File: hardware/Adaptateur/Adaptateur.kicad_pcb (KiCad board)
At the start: 2 copper layers, 74 x 42 mm, 16 parts, among them J1 USB_B, U1 FT232RL, U2 XBee, U3 IFX27001TFV33

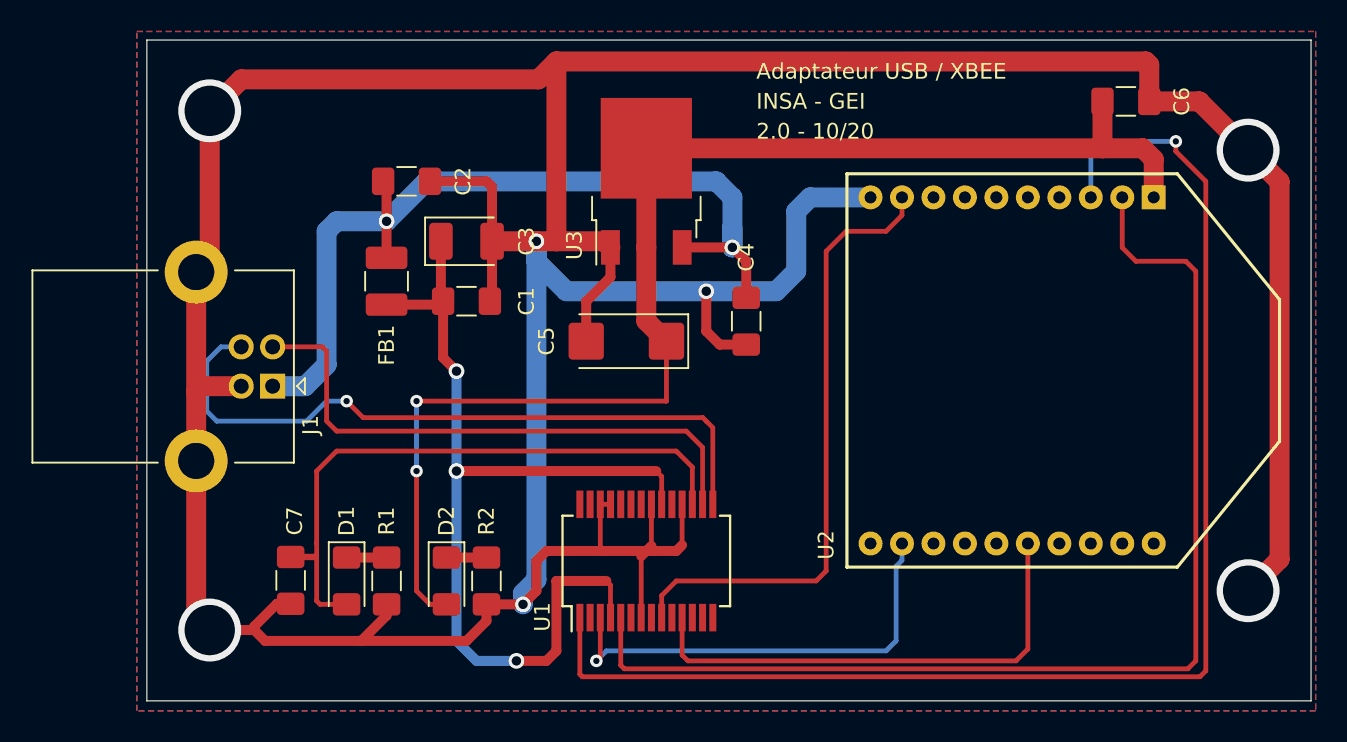
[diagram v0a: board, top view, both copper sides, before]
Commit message: correction et mise à jour adaptateur USB XBEE premiere version (boitier gris)
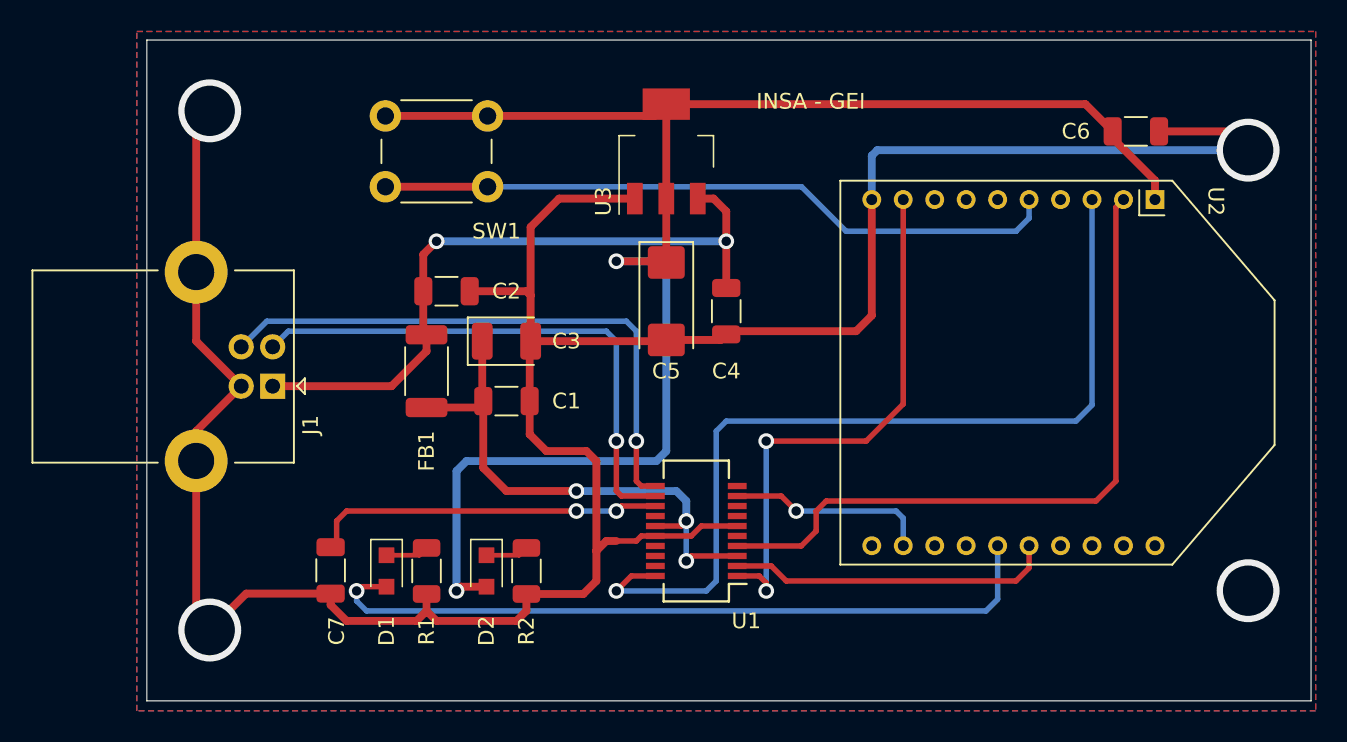
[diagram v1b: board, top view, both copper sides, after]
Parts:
- added SW1: SW_Push_SPDT, Button_Switch_THT:SW_PUSH_6mm_H5mm, F.Cu at (75.2, 74.8)
- C1, C2, C4, C6, C7: footprint Capacitor_SMD:C_1206_3216Metric_Pad1.42x1.75mm_HandSolder -> Capacitor_SMD:C_1206_3216Metric
- C3: footprint Capacitor_Tantalum_SMD:CP_EIA-3528-21_Kemet-B_Pad1.50x2.35mm_HandSolder -> Capacitor_Tantalum_SMD:CP_EIA-3528-21_Kemet-B
- C5: footprint Capacitor_Tantalum_SMD:CP_EIA-6032-28_Kemet-C_Pad2.25x2.35mm_HandSolder -> Capacitor_Tantalum_SMD:CP_EIA-6032-28_Kemet-C
- D1, D2: footprint LED_SMD:LED_1206_3216Metric_Pad1.42x1.75mm_HandSolder -> LED_SMD:LED_1206_3216Metric
- FB1: footprint Resistor_SMD:R_1210_3225Metric_Pad1.42x2.65mm_HandSolder -> Resistor_SMD:R_2010_5025Metric
- R1, R2: footprint Resistor_SMD:R_1206_3216Metric_Pad1.42x1.75mm_HandSolder -> Resistor_SMD:R_1206_3216Metric
- U1: value FT232RL -> FT231XS; footprint Package_SO:SSOP-28_5.3x10.2mm_P0.65mm -> Package_SO:SSOP-20_3.9x8.7mm_P0.635mm
- U2: value XBee -> XBEE-3-TH; footprint Insa:Xbee3 -> INSA:XBEE-3-TH
- U3: value IFX27001TFV33 -> NCP1117-3.3_SOT223; footprint Package_TO_SOT_SMD:TO-252-3_TabPin2 -> Package_TO_SOT_SMD:SOT-223-3_TabPin2
- moved U2 18.4 mm to (104.1, 78.9)
- moved C2 7.43 mm to (79.0, 86.0)
- moved C1 6.84 mm to (82.9, 93.0)
- moved C3 6.84 mm to (82.9, 89.1)
- moved FB1 6.25 mm to (77.8, 91.0)
- moved U1 3.70 mm to (94.9, 101.2), turned to 180 degrees
- moved C5 3.59 mm to (93.0, 86.6), turned to -90 degrees
- moved D2 2.62 mm to (81.6, 103.7)
- moved R1 2.62 mm to (77.8, 103.7)
- moved C7 2.62 mm to (71.7, 103.7)
- moved D1 2.62 mm to (75.2, 103.7)
- moved R2 2.62 mm to (84.1, 103.7)
- moved U3 2.29 mm to (93.0, 77.1)
- moved C6 2.01 mm to (122.9, 75.8)
- moved C4 1.42 mm to (96.8, 87.2)
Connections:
- net +3V3 renamed +3.3V
- D1 pad 2: Net-(C7-Pad1) -> Net-(D1-Pad2)
- U1 pad 1: /USART_TXD -> /USART_DTR
- U1 pad 10: Net-(U1-Pad10) -> unconnected-(U1-Pad10)
- U1 pad 11: /USART_CTS -> /USB_DP
- U1 pad 12: Net-(U1-Pad12) -> /USB_DM
- U1 pad 13: Net-(U1-Pad13) -> Net-(C7-Pad1)
- U1 pad 14: Net-(U1-Pad14) -> unconnected-(U1-Pad14)
- U1 pad 15: /USB_DP -> +5V
- U1 pad 16: /USB_DM -> GND
- U1 pad 17: Net-(C7-Pad1) -> unconnected-(U1-Pad17)
- U1 pad 18: GND -> unconnected-(U1-Pad18)
- U1 pad 19: Net-(U1-Pad19) -> unconnected-(U1-Pad19)
- U1 pad 2: Net-(U1-Pad2) -> /USART_RTS
- U1 pad 20: +5V -> /USART_TXD
- U1 pad 3: /USART_RTS -> +5V
- U1 pad 4: +5V -> /USART_RXD
- U1 pad 5: /USART_RXD -> unconnected-(U1-Pad5)
- U1 pad 6: Net-(U1-Pad6) -> GND
- U1 pad 7: GND -> unconnected-(U1-Pad7)
- U1 pad 8: (no net) -> unconnected-(U1-Pad8)
- U1 pad 9: /USART_DCR -> /USART_CTS
- U2 pad 11: Net-(U2-Pad11) -> unconnected-(U2-Pad11)
- U2 pad 12: /USART_RTS -> /USART_CTS
- U2 pad 13: Net-(U2-Pad13) -> unconnected-(U2-Pad13)
- U2 pad 14: Net-(U2-Pad14) -> (no net)
- U2 pad 15: Net-(U2-Pad15) -> Net-(D1-Pad2)
- U2 pad 16: /USART_CTS -> /USART_RTS
- U2 pad 17: Net-(U2-Pad17) -> unconnected-(U2-Pad17)
- U2 pad 18: Net-(U2-Pad18) -> unconnected-(U2-Pad18)
- U2 pad 19: Net-(U2-Pad19) -> unconnected-(U2-Pad19)
- U2 pad 20: Net-(U2-Pad20) -> unconnected-(U2-Pad20)
- U2 pad 4: Net-(U2-Pad4) -> unconnected-(U2-Pad4)
- U2 pad 6: Net-(U2-Pad6) -> unconnected-(U2-Pad6)
- U2 pad 7: Net-(U2-Pad7) -> unconnected-(U2-Pad7)
- U2 pad 8: Net-(U2-Pad8) -> (no net)
- U2 pad 9: /USART_DCR -> /USART_DTR
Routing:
- net GND: track 285.2 -> 175.5 mm, vias 7 -> 4
- net Net-(D1-Pad2): track 0.00 -> 47.4 mm, vias 0 -> 1
- net Net-(U2-Pad5): track 0.00 -> 43.6 mm
- net /USART_DCR: track 39.7 -> 0.00 mm
- net /USART_DTR: track 0.00 -> 34.7 mm, vias 0 -> 2
- net /USART_TXD: track 86.8 -> 56.6 mm
- net /USART_RXD: track 73.1 -> 44.6 mm
- net +5V: track 61.6 -> 34.9 mm
- net /USART_CTS: track 31.5 -> 12.9 mm, vias 0 -> 1
- net +3.3V: track 86.5 -> 104.3 mm
- net Net-(C7-Pad1): track 39.0 -> 22.5 mm, vias 0 -> 2
- net VCC: track 56.5 -> 43.6 mm
- net /USART_RTS: track 28.8 -> 20.7 mm, vias 1 -> 0
- net /USB_DP: track 44.3 -> 36.9 mm
- net /USB_DM: track 36.2 -> 34.7 mm, vias 0 -> 1
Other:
- net class Default removed
- board text removed: "2.0 - 10/20"
- board text removed: "Adaptateur USB / XBEE"

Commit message: Commit avant nouveau projet
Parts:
- added H1: MountingHole_Pad, MountingHole:MountingHole_3.2mm_M3_DIN965_Pad, F.Cu at (64.0, 74.5)
- added H2: MountingHole_Pad, MountingHole:MountingHole_3.2mm_M3_DIN965_Pad, F.Cu at (64.0, 107.5)
- added H3: MountingHole_Pad, MountingHole:MountingHole_3.2mm_M3_DIN965_Pad, F.Cu at (130.0, 77.0)
- added H4: MountingHole_Pad, MountingHole:MountingHole_3.2mm_M3_DIN965_Pad, F.Cu at (130.0, 105.0)
- added R3: 10K, Resistor_SMD:R_1206_3216Metric, F.Cu at (86.7, 75.8)
- SW1: value SW_Push_SPDT -> SW_DPST_x2; footprint Button_Switch_THT:SW_PUSH_6mm_H5mm -> Button_Switch_THT:SW_PUSH_6mm_H4.3mm
- moved SW1 7.91 mm to (81.7, 79.3), turned to 180 degrees
- moved C7 0.25 mm to (71.4, 103.7)
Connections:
- SW1 pad 1: +3.3V -> Net-(R3-Pad1)
- SW1 pad 2: Net-(U2-Pad5) -> GND
- U2 pad 5: Net-(U2-Pad5) -> Net-(R3-Pad1)
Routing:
- net Net-(R3-Pad1): track 0.00 -> 49.5 mm
- net Net-(U2-Pad5): track 43.6 -> 0.00 mm
- net +3.3V: track 104.3 -> 92.6 mm
- net GND: track 175.5 -> 182.0 mm, vias 4 -> 0
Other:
- board text added: "INSA - GEI V 2.1 - 12/22"
- board text removed: "INSA - GEI"
